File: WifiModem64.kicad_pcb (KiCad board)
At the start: 2 copper layers, 4 parts, among them J1 C64-UserPort, J2 PWR1, U1 WeMos_mini, U2 WeMos_D1_mini_OLED_Shield

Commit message: WiP.
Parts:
- removed J2: PWR1, Pin_Headers:Pin_Header_Straight_1x02_Pitch2.54mm
- added JP1: IntPwr, Connectors:GS2, F.Cu at (171.4, 105.9)
- added JP2: CTS, Connectors:GS2, B.Cu at (155.6, 114.3)
- added JP3: RTS, Connectors:GS2, B.Cu at (135.9, 114.3)
- added JP4: SP1, Connectors:GS2, B.Cu at (127.6, 109.6)
- added JP5: SP2, Connectors:GS2, B.Cu at (163.8, 109.6)
- added Q1: BSS138, TO_SOT_Packages_SMD:SOT-23, B.Cu at (158.6, 114.0)
- added Q2: BSS138, TO_SOT_Packages_SMD:SOT-23, B.Cu at (138.9, 114.0)
- added Q3: BSS138, TO_SOT_Packages_SMD:SOT-23, B.Cu at (130.7, 109.3)
- added Q4: BSS138, TO_SOT_Packages_SMD:SOT-23, B.Cu at (166.8, 109.3)
- added R1: 10k, Resistors_SMD:R_0805_HandSoldering, B.Cu at (157.9, 116.8)
- added R2: 10k, Resistors_SMD:R_0805_HandSoldering, B.Cu at (138.2, 116.8)
- added R3: 10k, Resistors_SMD:R_0805_HandSoldering, B.Cu at (129.9, 112.1)
- added R4: 10k, Resistors_SMD:R_0805_HandSoldering, B.Cu at (166.1, 112.1)
- added R5: 10k, Resistors_SMD:R_0805_HandSoldering, B.Cu at (161.4, 114.6)
- added R6: 10k, Resistors_SMD:R_0805_HandSoldering, B.Cu at (141.7, 114.6)
- added R7: 10k, Resistors_SMD:R_0805_HandSoldering, B.Cu at (133.5, 109.9)
- added R8: 10k, Resistors_SMD:R_0805_HandSoldering, B.Cu at (169.6, 109.9)
- moved U2 5.59 mm to (132.1, 95.2)
- moved U1 2.84 mm to (160.0, 95.2), turned to 180 degrees
- moved J1 2.65 mm to (146.6, 125.2)
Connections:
- net W_3V3 renamed +3V3
- net W_5V renamed +5V
- net W_GND renamed GND
- J1 pad 5: W_RX -> SP1
- J1 pad 7: W_TX -> SP2
- J1 pad B: W_TX -> SP2
- J1 pad C: W_TX -> SP2
- J1 pad D: W_D1 -> CTS
- J1 pad K: W_D2 -> RTS
- J1 pad M: W_RX -> SP1
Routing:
- net W_TX: track 79.5 -> 29.0 mm, vias 3 -> 0
- net W_RST: track 68.1 -> 29.0 mm, vias 2 -> 0
- net W_A0: track 63.0 -> 29.0 mm, vias 2 -> 0
- net +3V3: track 61.4 -> 29.0 mm, vias 2 -> 0
- net W_D1: track 59.9 -> 29.0 mm, vias 1 -> 0
- net W_D0: track 58.2 -> 29.0 mm, vias 2 -> 0
- net W_D8: track 57.5 -> 29.0 mm, vias 2 -> 0
- net Net-(J1-Pad6): track 28.3 -> 0.00 mm, vias 1 -> 0
- net W_D5: track 54.2 -> 29.0 mm, vias 2 -> 0
- net W_D7: track 53.6 -> 29.0 mm, vias 2 -> 0
- net W_D6: track 51.3 -> 29.0 mm
- net +5V: track 50.2 -> 29.0 mm, vias 1 -> 0
- net W_RX: track 49.7 -> 29.0 mm, vias 1 -> 0
- net W_D3: track 9.19 -> 29.0 mm
- net W_D4: track 11.8 -> 29.0 mm
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
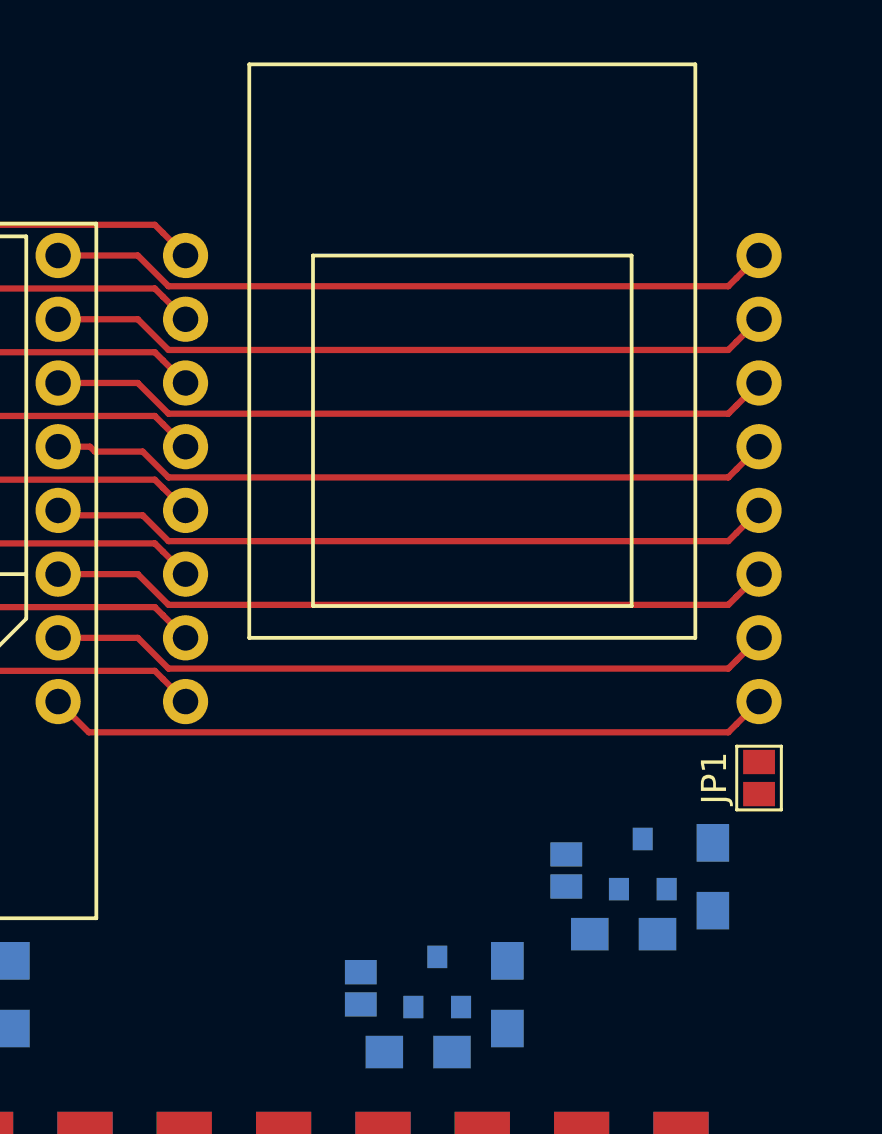
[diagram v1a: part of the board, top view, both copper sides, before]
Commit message: Optimized silk screen.
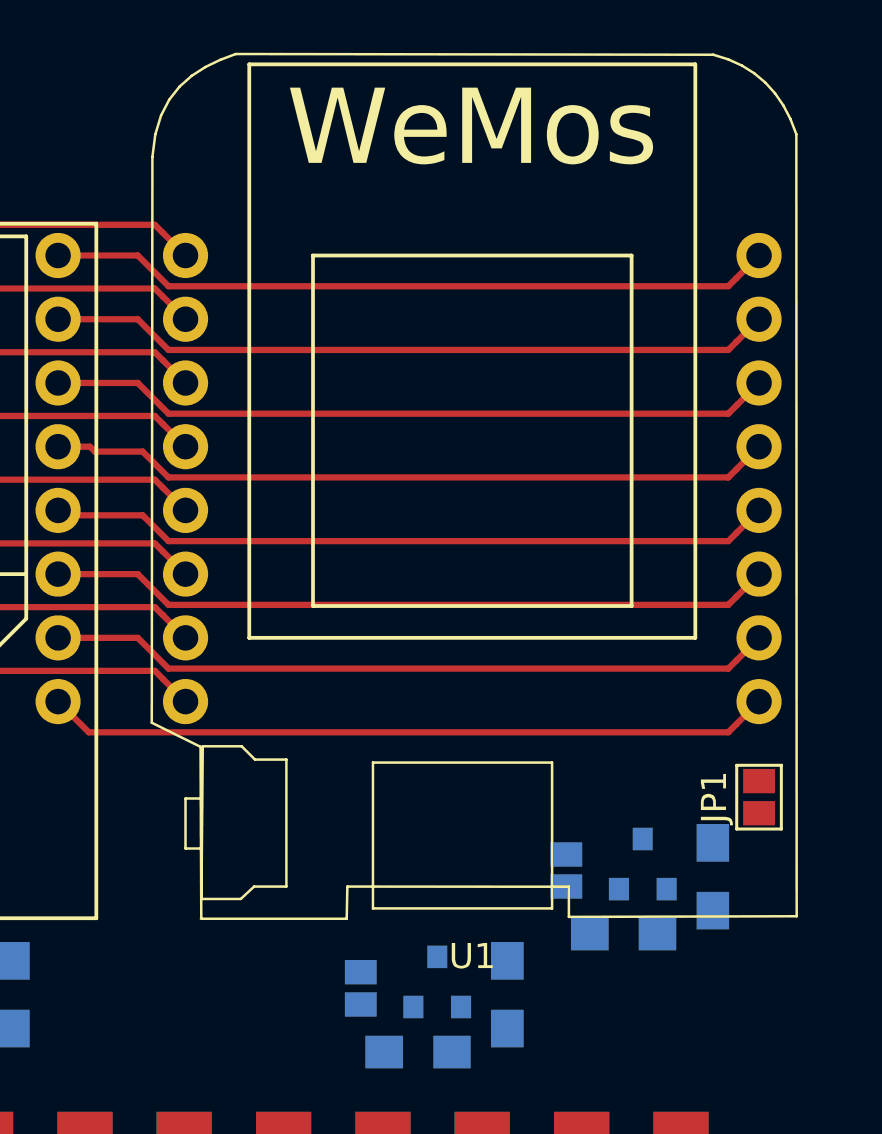
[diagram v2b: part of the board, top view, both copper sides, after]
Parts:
- U1: moved to F.Cu
- moved JP1 0.76 mm to (171.4, 106.7)
- turned U1 to 0 degrees

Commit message: WiP.
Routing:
- net +5V: track 29.0 -> 127.5 mm, vias 0 -> 4
- net +3V3: track 29.0 -> 98.9 mm, vias 0 -> 4
- net Net-(J1-Pad2): track 0.00 -> 17.8 mm
- net SP2: track 0.00 -> 14.8 mm
- net SP1: track 0.00 -> 14.7 mm
- net RTS: track 0.00 -> 10.0 mm
- net CTS: track 0.00 -> 9.97 mm
- net W_D7: track 29.0 -> 35.1 mm
- net W_RX: track 29.0 -> 35.1 mm
- net W_TX: track 29.0 -> 35.1 mm
- net W_D6: track 29.0 -> 35.1 mm

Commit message: WiP.
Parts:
- added REF**: VIA-0.6mm, hackup:VIA-0.6mm, F.Cu at (124.7, 117.3)
- added REF**: VIA-0.6mm, hackup:VIA-0.6mm, F.Cu at (132.3, 117.3)
- added REF**: VIA-0.6mm, hackup:VIA-0.6mm, F.Cu at (140.0, 103.9)
- added REF**: VIA-0.6mm, hackup:VIA-0.6mm, F.Cu at (140.0, 100.3)
- added Reset: Reset, Buttons_Switches_THT:SW_Tactile_SPST_Angled_PTS645Vx58-2LFS, F.Cu at (165.7, 69.8)
- added SW1: Push, Buttons_Switches_THT:SW_Tactile_SPST_Angled_PTS645Vx58-2LFS, F.Cu at (123.2, 69.8)
- moved J1 1.78 mm to (146.7, 127.0)
- moved JP1 0.64 mm to (172.1, 106.7)
- moved U1 0.63 mm to (160.7, 95.2)
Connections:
- J1 pad 3: Net-(J1-Pad3) -> RST
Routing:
- net RST: track 0.00 -> 58.1 mm, vias 0 -> 1
- net W_D3: track 29.0 -> 68.5 mm
- net SP1: track 14.7 -> 47.9 mm, vias 0 -> 3
- net SP2: track 14.8 -> 43.9 mm, vias 0 -> 1
- net W_RX: track 35.1 -> 60.8 mm
- net W_TX: track 35.1 -> 60.4 mm
- net Net-(J1-Pad6): track 0.00 -> 22.4 mm, vias 0 -> 3
- net W_D6: track 35.1 -> 56.6 mm
- net W_D7: track 35.1 -> 54.5 mm
- net +5V: track 127.5 -> 130.7 mm
- net Net-(J1-Pad2): track 17.8 -> 19.8 mm
- net RTS: track 10.0 -> 12.0 mm
- net CTS: track 9.97 -> 11.8 mm
- net +3V3: track 98.9 -> 99.9 mm
- net W_D2: track 29.0 -> 29.6 mm
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- added copper zone on B.Cu, net GND
- added copper zone on F.Cu, net GND
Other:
- board outline added: 55.9 x 59.7 mm
- board text added: "V0.9"
- board text added: "WifiModem64"
- board text added: "github.com/hackup/WifiModem64"

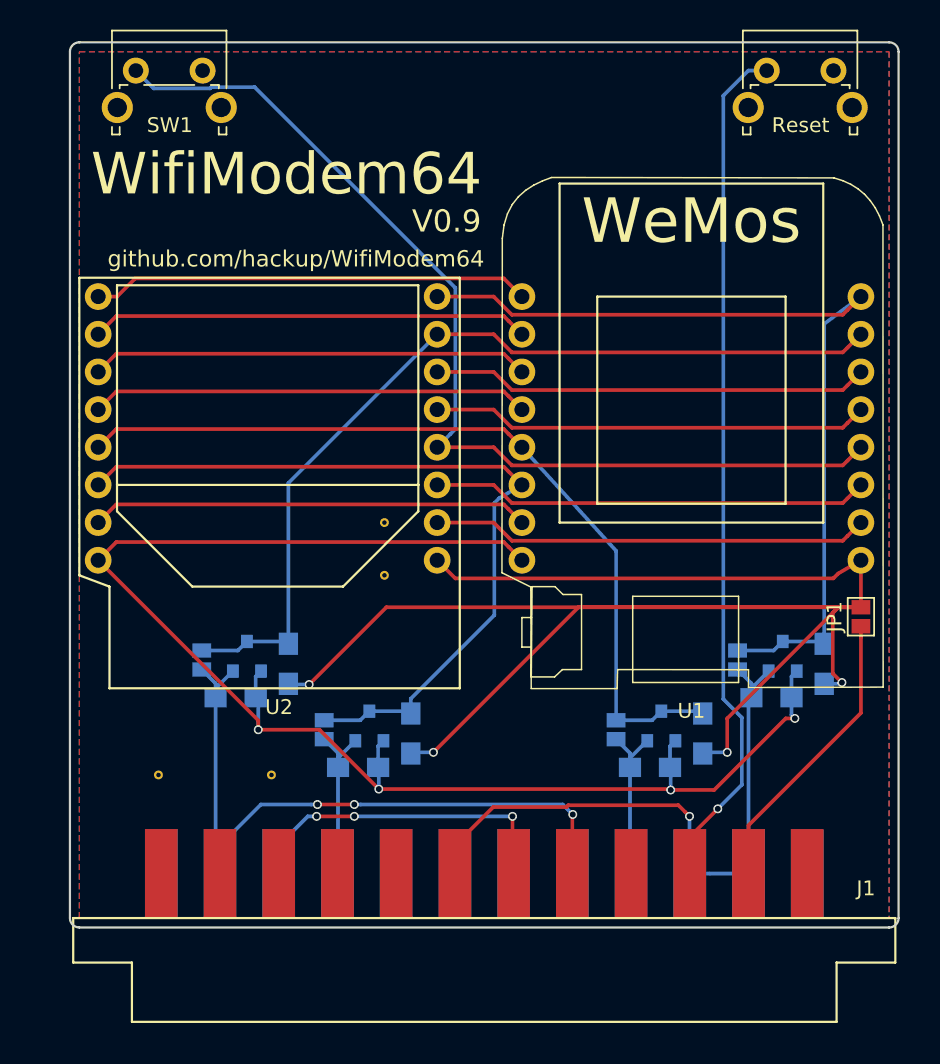
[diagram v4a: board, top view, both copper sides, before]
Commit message: Added LED and mounting holes.
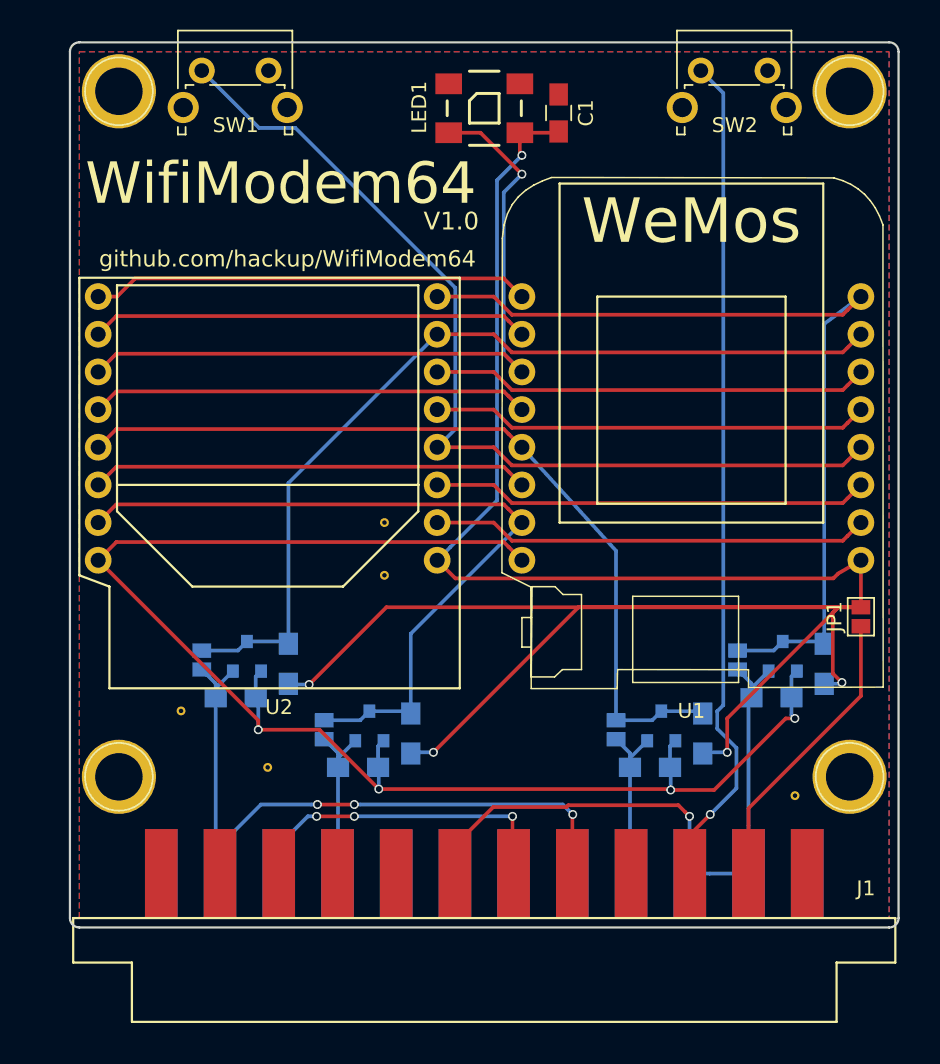
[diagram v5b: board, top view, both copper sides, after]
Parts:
- added C1: 100n, Capacitors_SMD:C_0805_HandSoldering, F.Cu at (151.7, 72.7)
- added LED1: WS2812B, WifiModem64:WS2812B, F.Cu at (146.7, 72.4)
- added REF**: VIA-0.6mm, hackup:VIA-0.6mm, F.Cu at (167.6, 118.7)
- added REF**: 1pin, Connectors:1pin, F.Cu at (171.3, 71.2)
- added REF**: 1pin, Connectors:1pin, F.Cu at (122.0, 71.2)
- added REF**: 1pin, Connectors:1pin, F.Cu at (171.3, 117.5)
- added REF**: 1pin, Connectors:1pin, F.Cu at (122.0, 117.5)
- moved REF** 4.58 mm to (126.2, 113.0)
- moved SW2 4.45 mm to (161.3, 69.8)
- moved SW1 4.45 mm to (127.6, 69.8)
- moved REF** 0.57 mm to (132.1, 116.8)
- renumbered Reset to SW2
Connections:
- JP3 pad 2: W_D7 -> W_D8
- Q2 pad 3: W_D7 -> W_D8
- R6 pad 2: W_D7 -> W_D8
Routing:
- net +5V: track 130.7 -> 164.6 mm, vias 4 -> 5
- net W_D7: track 54.5 -> 29.6 mm
- net W_D8: track 29.6 -> 51.7 mm
- net W_D0: track 29.6 -> 50.2 mm, vias 0 -> 1
- net W_D3: track 68.5 -> 64.0 mm
- net RST: track 58.1 -> 59.3 mm
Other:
- board text added: "CTS"
- board text added: "RTS"
- board text added: "RX"
- board text added: "TX"
- board text added: "V1.0"
- board text removed: "V0.9"

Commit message: Added optional USB power supply.
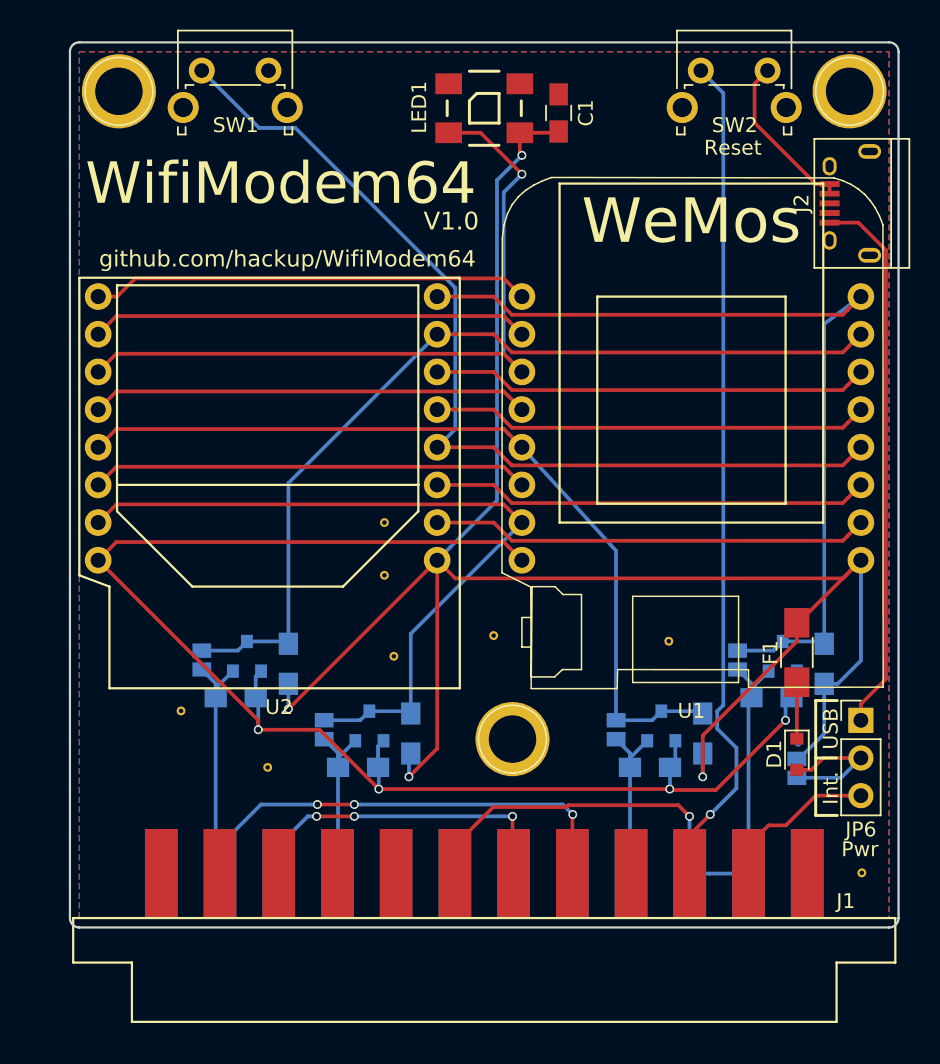
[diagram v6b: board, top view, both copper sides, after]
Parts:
- removed the REF** at (171.3, 117.5)
- added D1: B5819WS, Diodes_SMD:D_0805, F.Cu at (167.8, 116.0)
- added F1: 0.5A, Resistors_SMD:R_1206_HandSoldering, F.Cu at (167.8, 109.1)
- added J2: USB_B, Connectors:USB_Micro-B, F.Cu at (171.3, 78.8)
- added JP6: PwrSrc, Pin_Headers:Pin_Header_Straight_1x03_Pitch2.54mm, F.Cu at (172.1, 113.7)
- added REF**: VIA-0.6mm, hackup:VIA-0.6mm, F.Cu at (159.1, 108.3)
- added REF**: VIA-0.6mm, hackup:VIA-0.6mm, F.Cu at (140.6, 109.3)
- added REF**: VIA-0.6mm, hackup:VIA-0.6mm, F.Cu at (147.3, 108.0)
- JP1: value IntPwr -> PwrSafety; moved to B.Cu
- moved REF** 26.7 mm to (148.6, 114.9)
- moved JP1 11.1 mm to (167.8, 116.9)
- moved REF** 6.89 mm to (172.1, 124.0)
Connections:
- JP1 pad 1: Net-(J1-Pad2) -> +5V
- JP1 pad 2: +5V -> Net-(D1-Pad2)
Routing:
- net Net-(J2-Pad1): track 0.00 -> 37.0 mm
- net +5V: track 164.6 -> 133.1 mm, vias 5 -> 4
- net GND: track 29.6 -> 40.9 mm
- net Net-(D1-Pad2): track 0.00 -> 9.52 mm
- net Net-(J1-Pad2): track 19.8 -> 10.9 mm
- net Net-(D1-Pad1): track 0.00 -> 3.81 mm
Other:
- board text added: "Int."
- board text added: "Safety"
- board text added: "USB"
